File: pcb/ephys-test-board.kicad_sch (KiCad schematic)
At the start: 2 parts, among them J1 Conn_02x10_Odd_Even, J8 BM03B-SRSS-TB

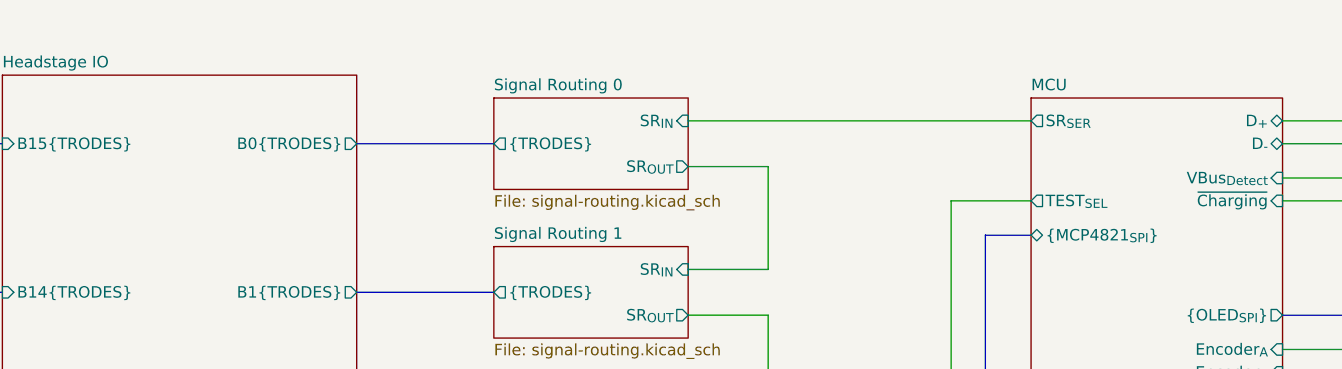
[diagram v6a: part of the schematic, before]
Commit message: Add EEPROM support to headstage interface
- I2C + Power
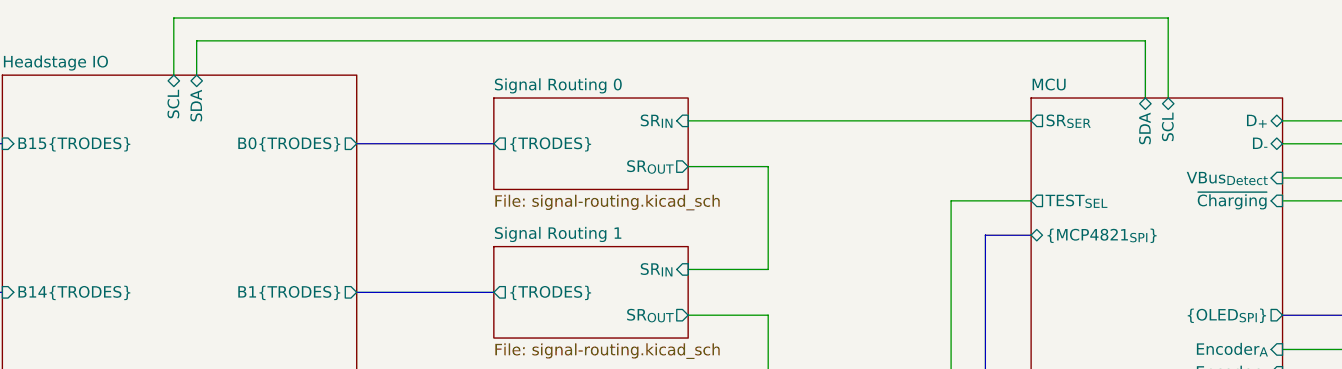
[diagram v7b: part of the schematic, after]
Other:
- sheet Headstage IO ports: added SCL, SDA; removed none
- sheet MCU ports: added SCL, SDA; removed none
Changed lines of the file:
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@@
 	(wire
 		(pts
+			(xy 204.47 26.67) (xy 93.98 26.67)
+		)
+		(stroke
+			(width 0)
+			(type default)
+		)
+	)
+	(wire
+		(pts
 			(xy 257.81 93.98) (xy 261.62 93.98)
 		)
@@
 	(wire
 		(pts
+			(xy 96.52 29.21) (xy 201.93 29.21)
+		)
+		(stroke
+			(width 0)
+			(type default)
+		)
+	)
+	(wire
+		(pts
 			(xy 261.62 104.14) (xy 261.62 106.68)
 		)
@@
 		)
 	)
+	(wire
+		(pts
+			(xy 204.47 35.56) (xy 204.47 26.67)
+		)
+		(stroke
+			(width 0)
+			(type default)
+		)
+	)
 	(bus
 		(pts
@@
 	(wire
 		(pts
+			(xy 96.52 33.02) (xy 96.52 29.21)
+		)
+		(stroke
+			(width 0)
+			(type default)
+		)
+	)
+	(wire
+		(pts
 			(xy 29.21 87.63) (xy 38.1 87.63)
 		)
@@
 	(wire
 		(pts
+			(xy 93.98 26.67) (xy 93.98 33.02)
+		)
+		(stroke
+			(width 0)
+			(type default)
+		)
+	)
+	(wire
+		(pts
 			(xy 217.17 86.36) (xy 245.11 86.36)
 		)
@@
 		)
 	)
+	(wire
+		(pts
+			(xy 201.93 29.21) (xy 201.93 35.56)
+		)
+		(stroke
+			(width 0)
+			(type default)
+		)
+	)
 	(bus
 		(pts
@@
 			)
 		)
+		(pin "SDA" bidirectional
+			(at 201.93 35.56 90)
+			(effects
+				(font
+					(size 1.27 1.27)
+				)
+				(justify right)
+			)
+		)
+		(pin "SCL" bidirectional
+			(at 204.47 35.56 90)
+			(effects
+				(font
+					(size 1.27 1.27)
+				)
+				(justify right)
+			)
+		)
 		(instances
 			(project "ephys-test-board"
@@
 			)
 		)
+		(pin "SCL" bidirectional
+			(at 93.98 33.02 90)
+			(effects
+				(font
+					(size 1.27 1.27)
+				)
+				(justify right)
+			)
+		)
+		(pin "SDA" bidirectional
+			(at 96.52 33.02 90)
+			(effects
+				(font
+					(size 1.27 1.27)
+				)
+				(justify right)
+			)
+		)

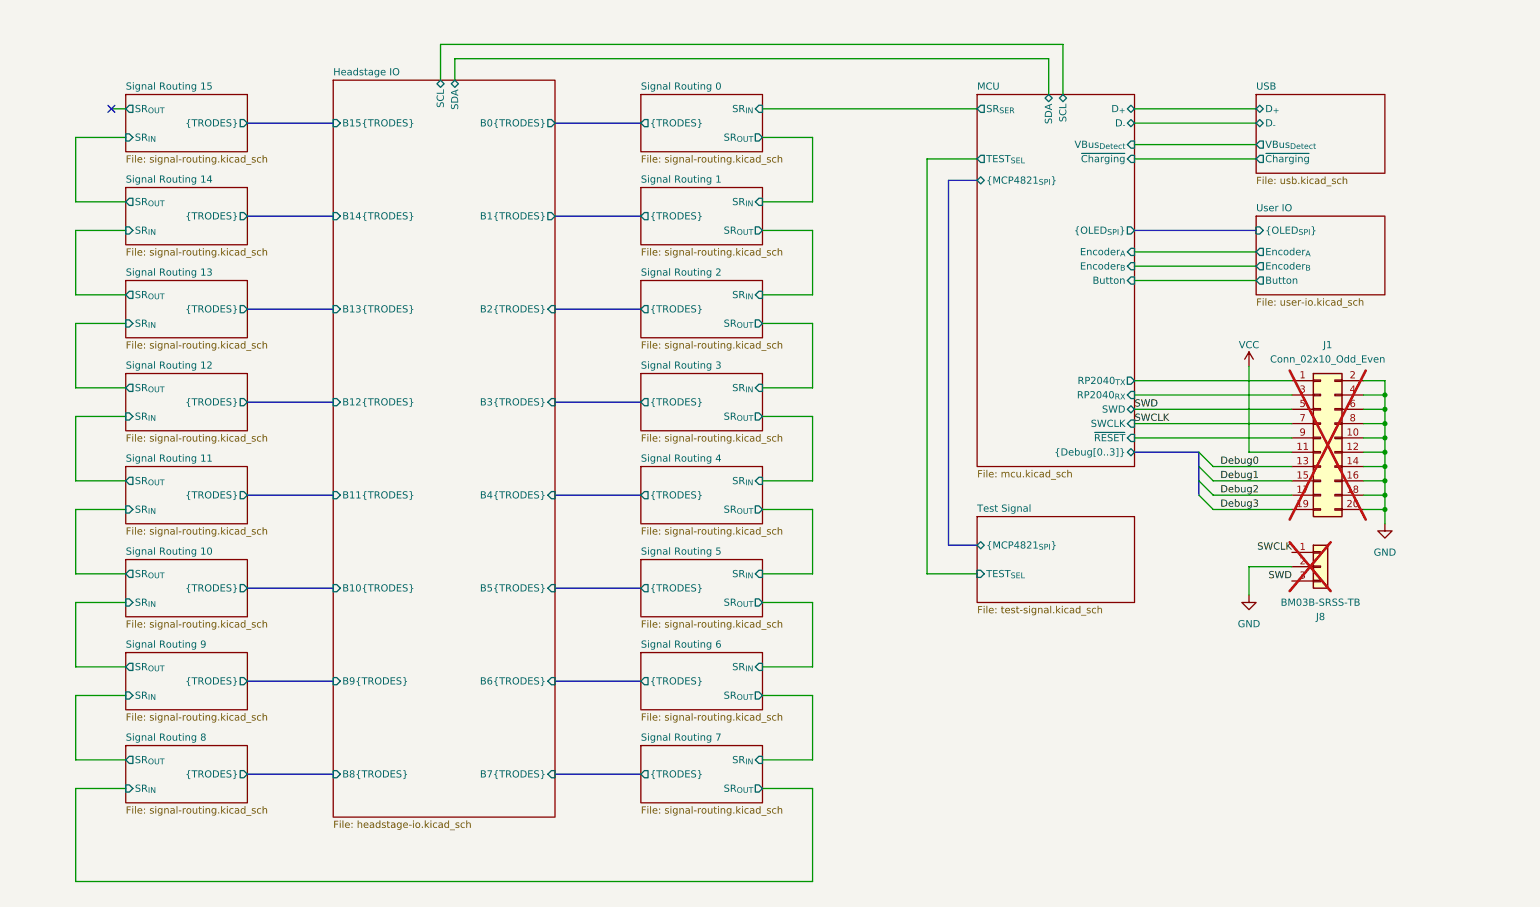
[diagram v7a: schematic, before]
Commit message: More schematic improvements
- Add pullups to i2c bus
- Add test points
- Ready for initial routing
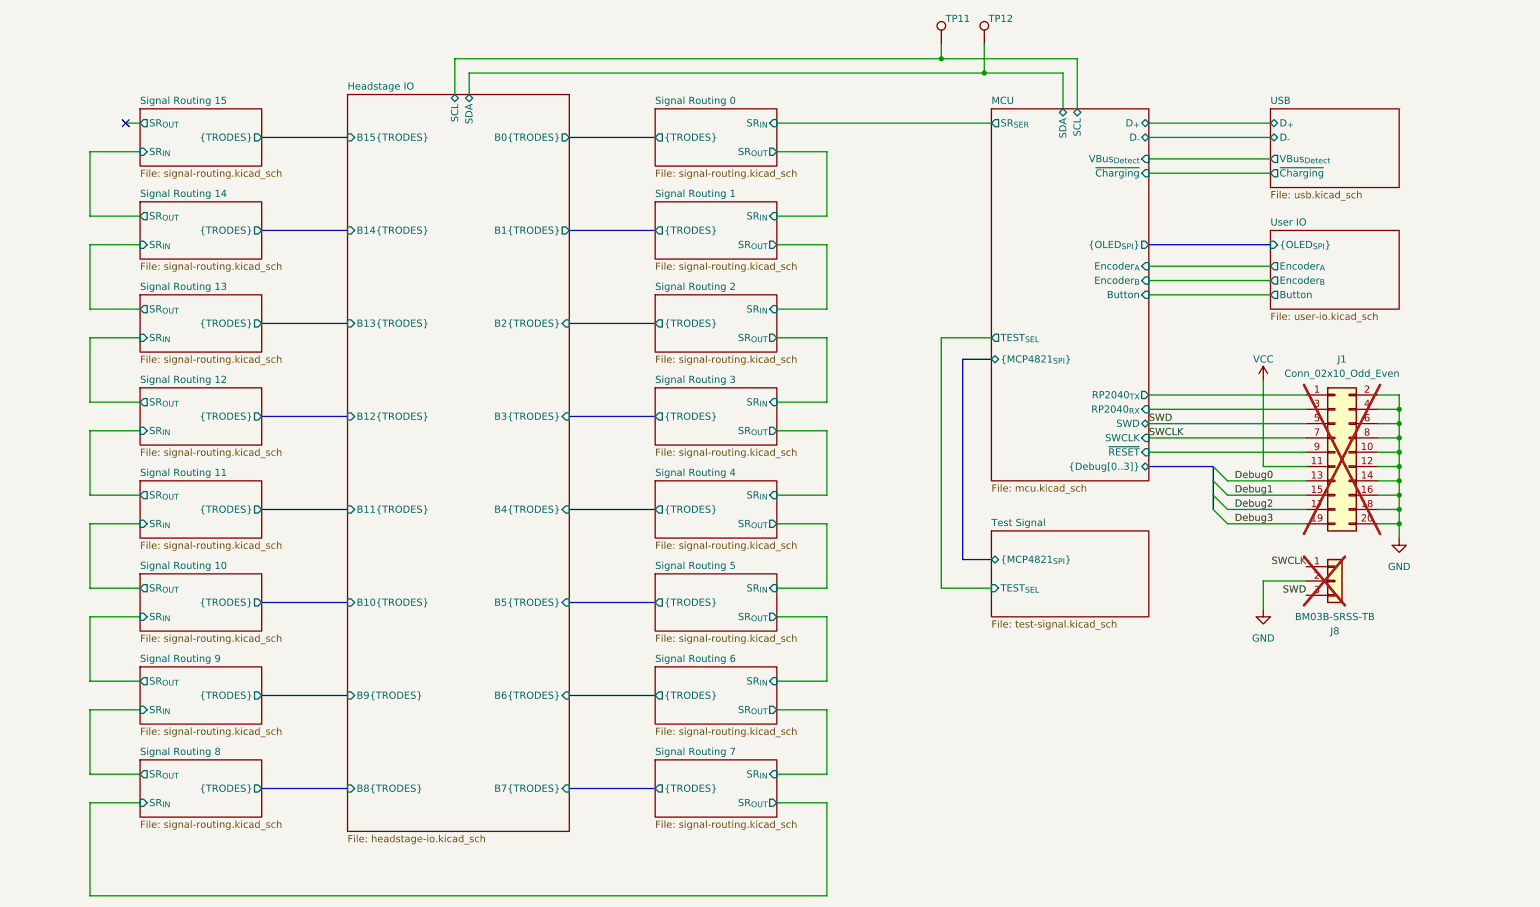
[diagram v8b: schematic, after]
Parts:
- added TP11, TP12: VCC, TestPoint:TestPoint_Pad_D2.0mm, symbol Connector:TestPoint
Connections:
- net Headstage IO/SCL: now also TP11.1
- net Headstage IO/SDA: now also TP12.1
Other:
- moved on the sheet: J1, J8
